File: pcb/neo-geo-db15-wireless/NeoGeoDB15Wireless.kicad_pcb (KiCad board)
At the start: 2 copper layers, 39.9 x 32 mm, 5 parts, among them J1 DB15_Female_MountingHoles, U1 RP2040-Zero, U2 NRF24L01

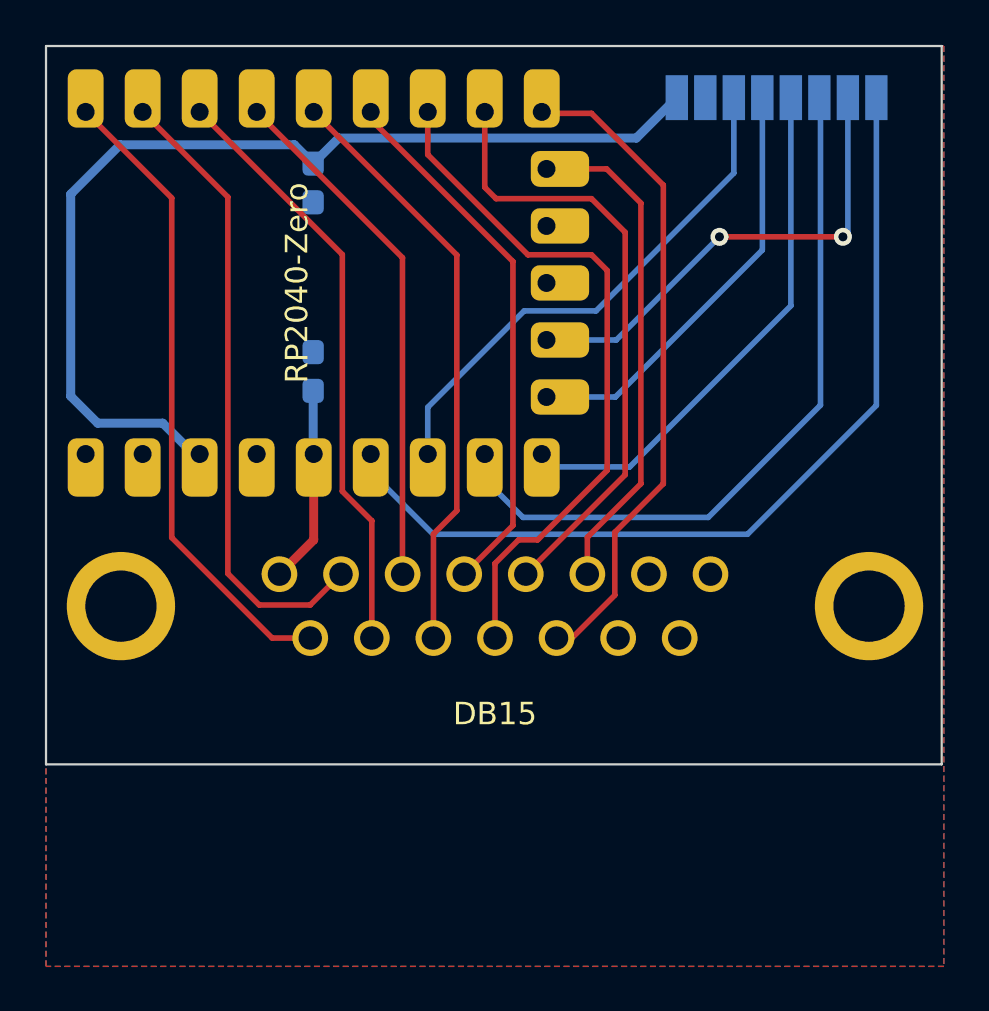
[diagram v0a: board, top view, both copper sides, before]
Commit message: Fixes errors in PCB, incorrect pin numbering on RP2040, unconnected grounds, ground mounting points, some vias to increase ground plane flood
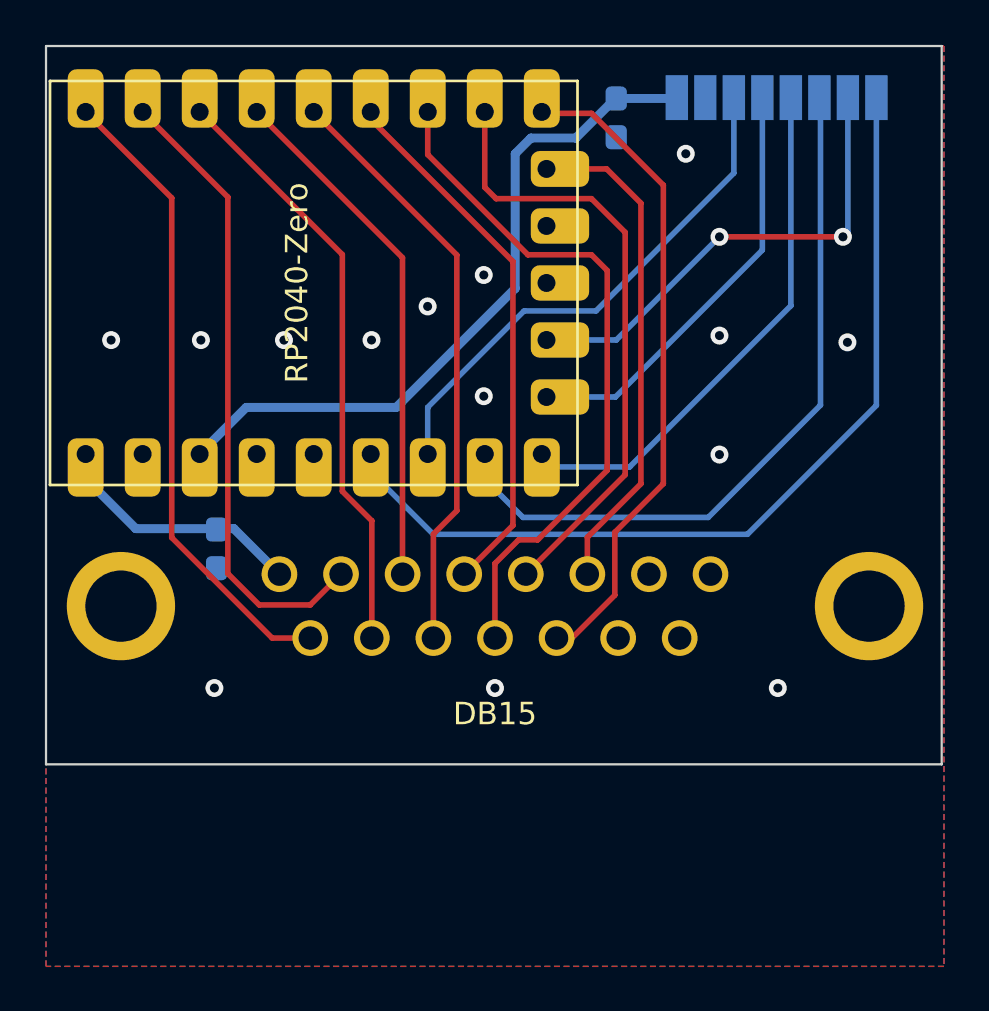
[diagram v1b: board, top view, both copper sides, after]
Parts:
- J1: value DB15_Female_MountingHoles -> DB15_F
- moved C2 13.8 mm to (105.4, 64.7)
- moved C1 8.99 mm to (87.6, 83.9), turned to -90 degrees
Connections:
- C1 pad 2: /GND -> GND
- C2 pad 2: /GND -> GND
- J1 pad 1: /GND -> GND
- U1 pad 22: /VCC -> GND
- U1 pad 23: /GND -> /VCC
- U2 pad 1: /GND -> GND
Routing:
- net /3V3: track 45.3 -> 31.3 mm
- net /VCC: track 8.81 -> 11.5 mm
- net GND: vias 0 -> 14
- added copper zone on B.Cu, net GND
- added copper zone on F.Cu, net GND
- removed copper zone on B.Cu, net /GND
- removed copper zone on F.Cu, net /GND

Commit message: Adds silk
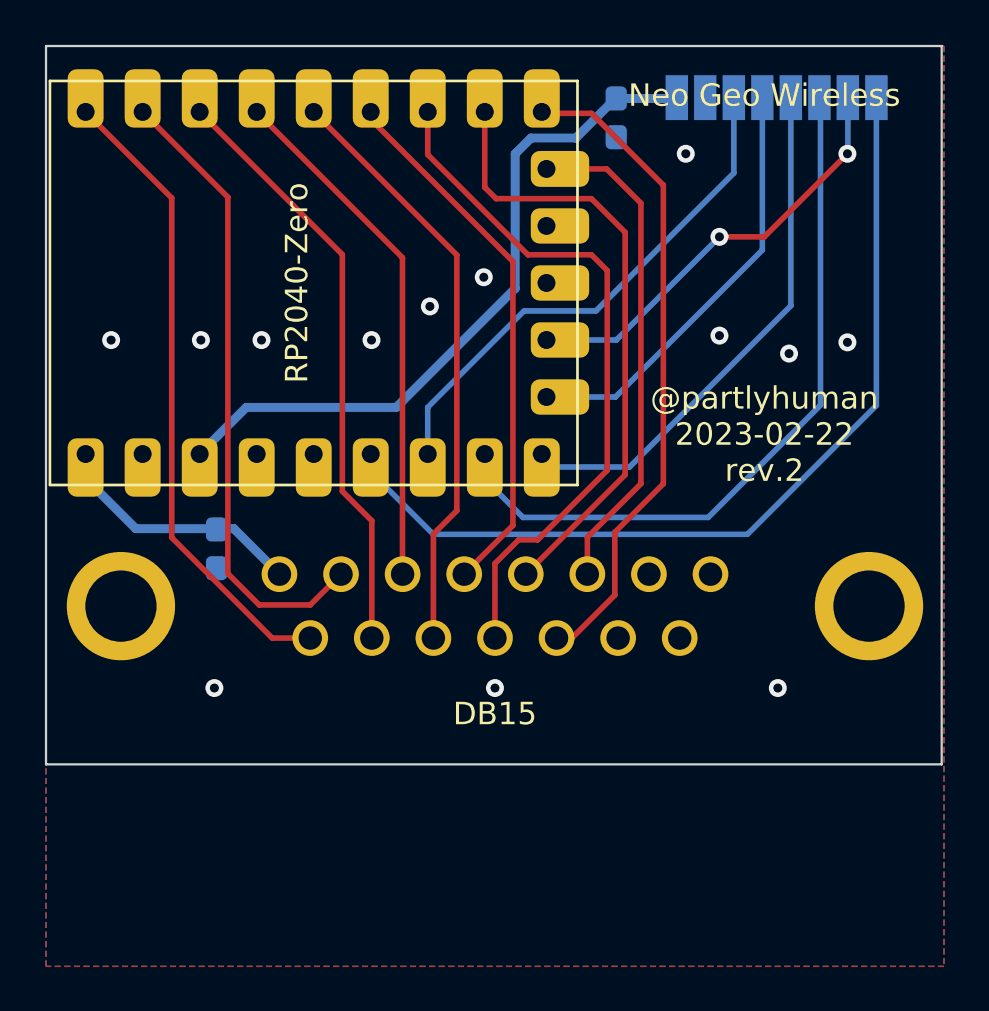
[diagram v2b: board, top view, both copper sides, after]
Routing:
- net /MISO: track 21.4 -> 19.3 mm
- net GND: vias 14 -> 13
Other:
- board text added: "${COMPANY} ${ISSUE_DATE} rev.${REVISION}"
- board text added: "Neo Geo Wireless"
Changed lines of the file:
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@@
   )
   (paper "A4")
+  (title_block
+    (title "Neo Geo Wireless Receiver")
+    (date "2023-02-22")
+    (rev "2")
+    (company "@partlyhuman")
+  )
   (layers
     (0 "F.Cu" signal)
@@
     (effects (font (size 1 1) (thickness 0.15)))
   )
+  (gr_text "${COMPANY}\n${ISSUE_DATE}\nrev.${REVISION}" (at 112 78.8) (layer "F.SilkS")
+    (effects (font (size 1 1) (thickness 0.15)))
+  )
+  (gr_text "Neo Geo Wireless" (at 112 63.7) (layer "F.SilkS")
+    (effects (font (size 1 1) (thickness 0.15)))
+  )
   (segment (start 88.370399 83) (end 90.398799 85.0284) (width 0.4) (layer "B.Cu") (net 3))
   (segment (start 84 83) (end 88.370399 83) (width 0.4) (layer "B.Cu") (net 3))
@@
   (segment (start 104.3 64.5) (end 102.15 64.5) (width 0.25) (layer "F.Cu") (net 14))
   (segment (start 103.4268 87.8732) (end 105.338194 85.961806) (width 0.25) (layer "F.Cu") (net 14))
-  (segment (start 110 70) (end 115.5 70) (width 0.25) (layer "F.Cu") (net 15))
+  (segment (start 112 70) (end 115.7 66.3) (width 0.25) (layer "F.Cu") (net 15))
+  (segment (start 110 70) (end 112 70) (width 0.25) (layer "F.Cu") (net 15))
   (via (at 110 70) (size 0.8) (drill 0.4) (layers "F.Cu" "B.Cu") (net 15))
-  (via (at 115.5 70) (size 0.8) (drill 0.4) (layers "F.Cu" "B.Cu") (net 15))
+  (via (at 115.7 66.3) (size 0.8) (drill 0.4) (layers "F.Cu" "B.Cu") (net 15))
+  (segment (start 115.72 66.28) (end 115.72 63.8) (width 0.25) (layer "B.Cu") (net 15))
+  (segment (start 115.7 66.3) (end 115.72 66.28) (width 0.25) (layer "B.Cu") (net 15))
   (segment (start 102.295 74.595) (end 105.405 74.595) (width 0.25) (layer "B.Cu") (net 15))
-  (segment (start 115.72 69.78) (end 115.72 63.8) (width 0.25) (layer "B.Cu") (net 15))
-  (segment (start 115.5 70) (end 115.72 69.78) (width 0.25) (layer "B.Cu") (net 15))
   (segment (start 105.405 74.595) (end 110 70) (width 0.25) (layer "B.Cu") (net 15))
   (segment (start 111.91 63.8) (end 111.91 70.59) (width 0.25) (layer "B.Cu") (net 16))
@@
   (via (at 82.9 74.6) (size 0.8) (drill 0.4) (layers "F.Cu" "B.Cu") (free) (net 26))
   (via (at 86.9 74.6) (size 0.8) (drill 0.4) (layers "F.Cu" "B.Cu") (free) (net 26))
-  (via (at 97 73.1) (size 0.8) (drill 0.4) (layers "F.Cu" "B.Cu") (free) (net 26))
+  (via (at 97.1 73.1) (size 0.8) (drill 0.4) (layers "F.Cu" "B.Cu") (free) (net 26))
   (via (at 87.5 90.1) (size 0.8) (drill 0.4) (layers "F.Cu" "B.Cu") (free) (net 26))
-  (via (at 99.5 71.7) (size 0.8) (drill 0.4) (layers "F.Cu" "B.Cu") (free) (net 26))
-  (via (at 99.5 77.1) (size 0.8) (drill 0.4) (layers "F.Cu" "B.Cu") (free) (net 26))
   (via (at 108.5 66.3) (size 0.8) (drill 0.4) (layers "F.Cu" "B.Cu") (free) (net 26))
   (via (at 100 90.1) (size 0.8) (drill 0.4) (layers "F.Cu" "B.Cu") (free) (net 26))
-  (via (at 110 79.7) (size 0.8) (drill 0.4) (layers "F.Cu" "B.Cu") (free) (net 26))
+  (via (at 113.1 75.2) (size 0.8) (drill 0.4) (layers "F.Cu" "B.Cu") (free) (net 26))
   (via (at 110 74.4) (size 0.8) (drill 0.4) (layers "F.Cu" "B.Cu") (free) (net 26))
+  (via (at 99.5 71.8) (size 0.8) (drill 0.4) (layers "F.Cu" "B.Cu") (free) (net 26))
   (via (at 112.6 90.1) (size 0.8) (drill 0.4) (layers "F.Cu" "B.Cu") (free) (net 26))
-  (via (at 90.6 74.6) (size 0.8) (drill 0.4) (layers "F.Cu" "B.Cu") (free) (net 26))
+  (via (at 89.6 74.6) (size 0.8) (drill 0.4) (layers "F.Cu" "B.Cu") (free) (net 26))
   (via (at 94.5 74.6) (size 0.8) (drill 0.4) (layers "F.Cu" "B.Cu") (free) (net 26))
   (zone (net 26) (net_name "GND") (layers F&B.Cu) (name "GroundPlane") (hatch edge 0.508)
